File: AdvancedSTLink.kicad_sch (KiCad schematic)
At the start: 66 parts, among them J1 Conn_01x03, J3 Conn_01x06, J4 USB_C_Receptacle_USB2.0, J5 Conn_01x05, Q1 S8050, SW1 SW_SPDT, SW2 SW_Push, U1 STM32F205RETx, U2 XC6206P332MR, U3 USBLC6-2P6, U4 GM9038, U5 USBLC6-2P6, U6 USBLC6-2P6, U7 CH340E, Y1 X322512MSB4SI

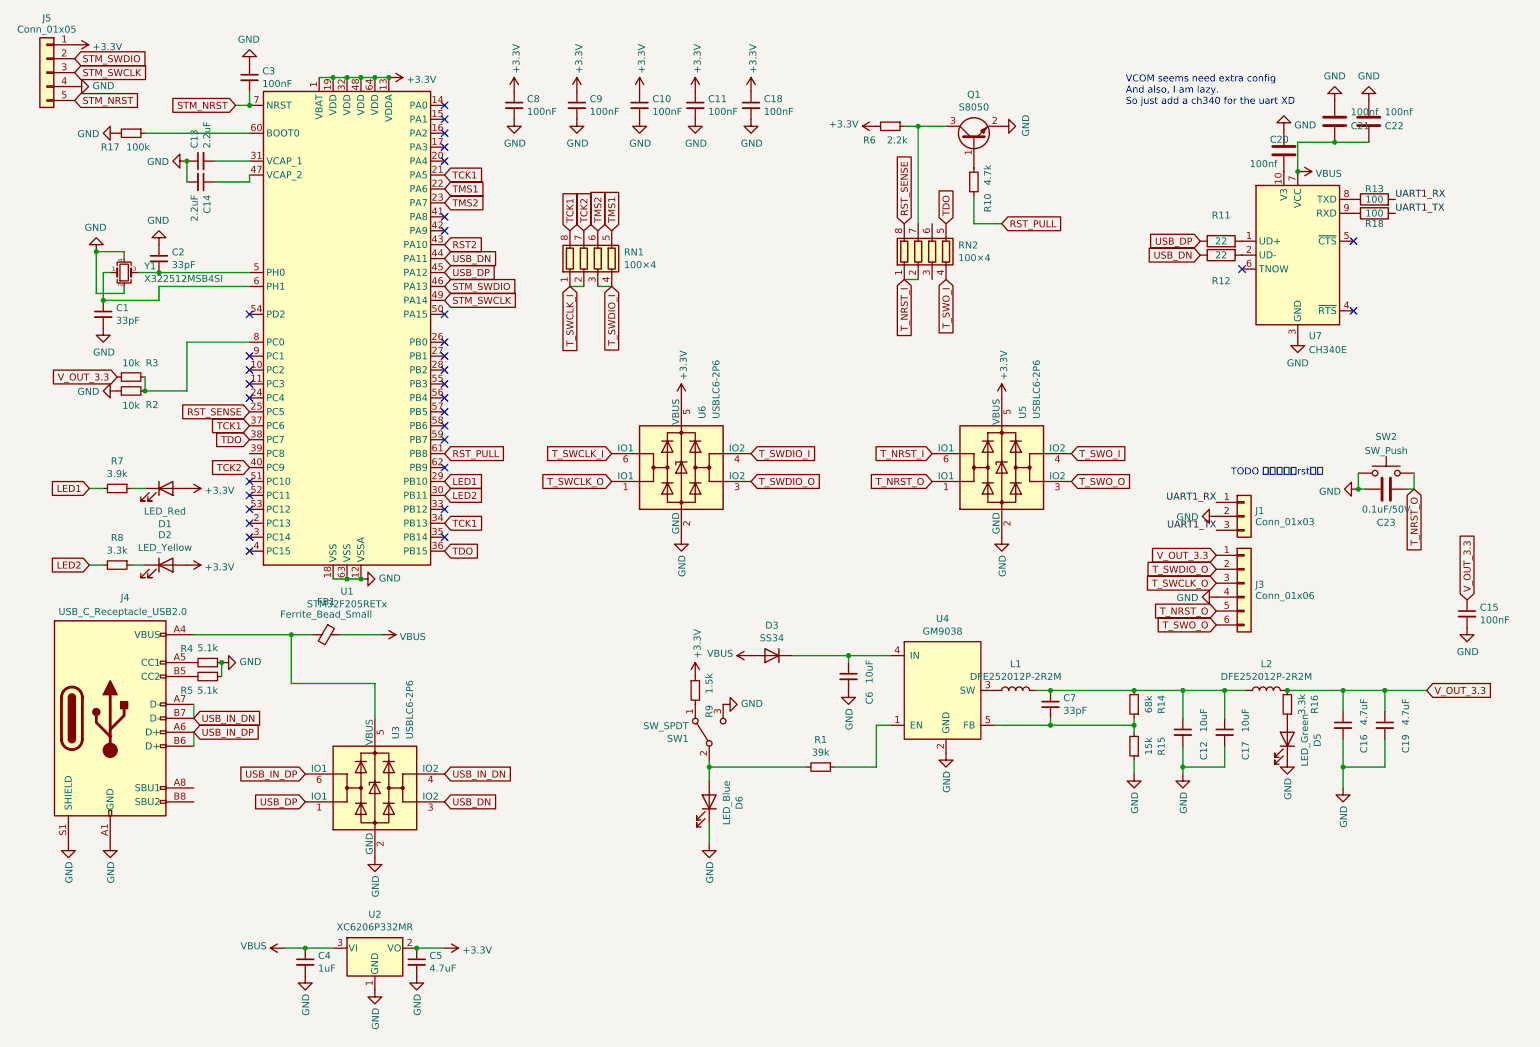
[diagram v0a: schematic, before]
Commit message: Remove CH340, use VCOM
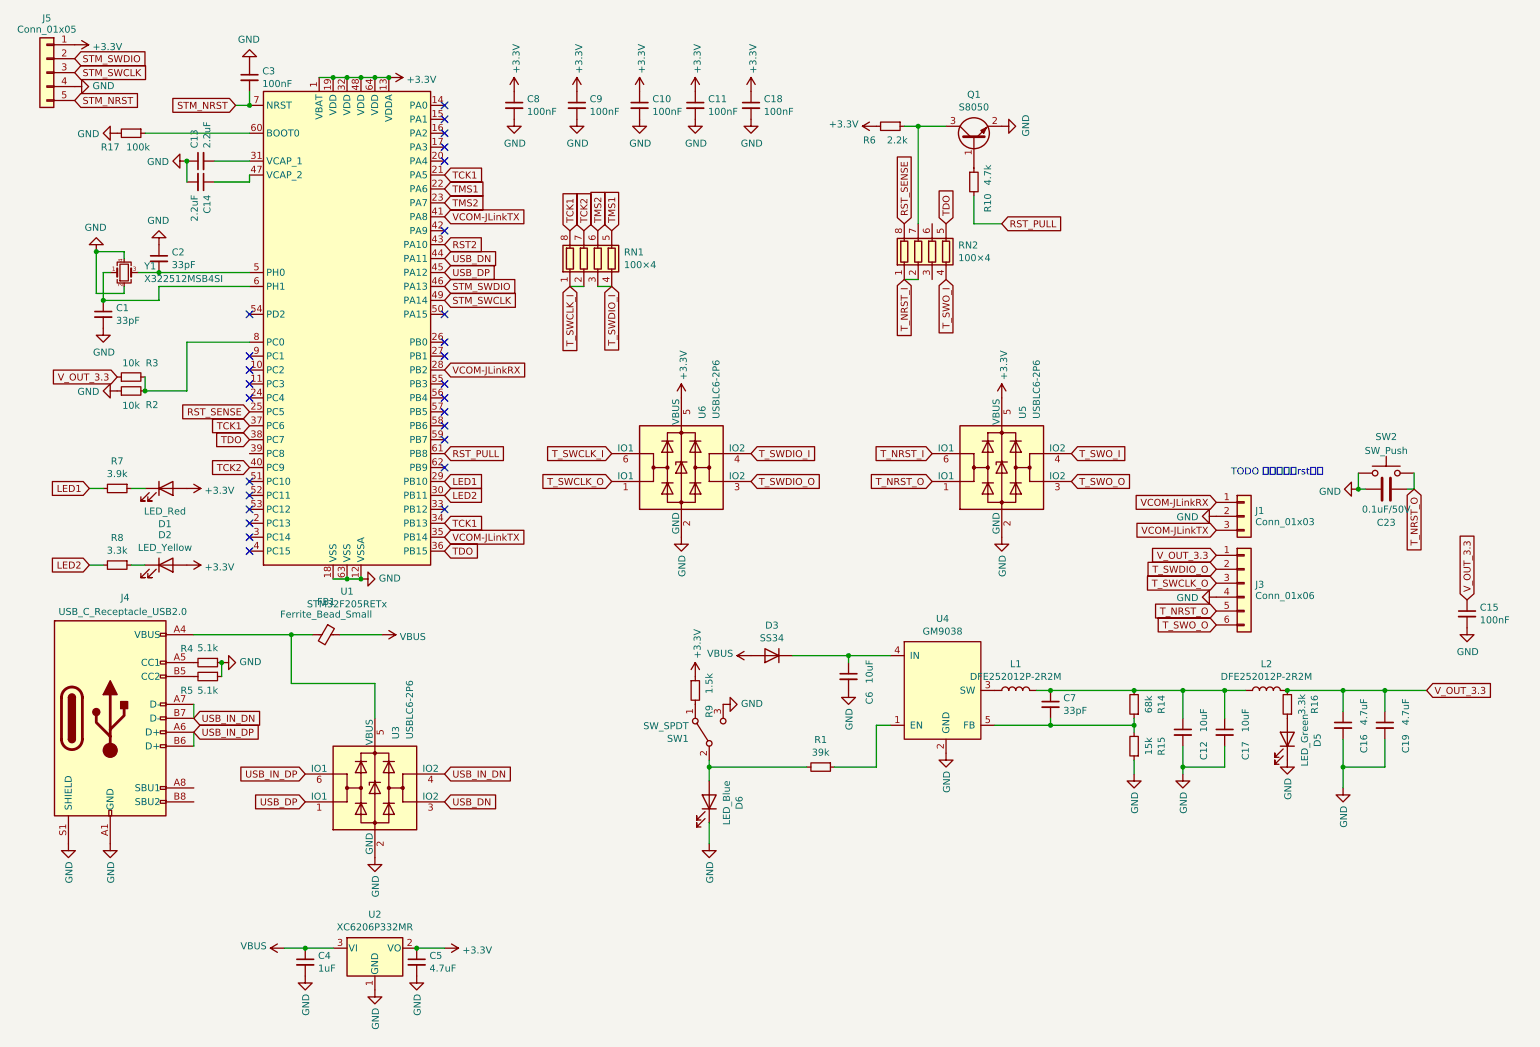
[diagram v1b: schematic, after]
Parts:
- removed C20, C21, C22: 100nf, Capacitor_SMD:C_0402_1005Metric, symbol Device:C
- removed R11, R12: 22, Resistor_SMD:R_0402_1005Metric, symbol Device:R
- removed R13, R18: 100, Resistor_SMD:R_0402_1005Metric, symbol Device:R
- removed U7: CH340E, Package_SO:MSOP-10_3x3mm_P0.5mm, symbol Interface_USB:CH340E
- SW2: footprint KisonNew:C393942 -> Button_Switch_SMD:SW_SPST_CK_RS282G05A3
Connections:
- net UART1_RX is gone; now on net VCOM-JLinkRX: J1.1 (Pin_1)
- net UART1_TX is gone; now on net VCOM-JLinkTX: J1.3 (Pin_3)
- net VCOM-JLinkRX: now reaches U1.28 (PB2)
- net VCOM-JLinkTX: now reaches U1.35 (PB14)
- net VCOM-JLinkTX: now also U1.41 (PA8)
- no-connect marks 33 -> 27
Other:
- note removed: "VCOM seems need extra config And also, I am lazy. So just add a ch340 for the uart XD"

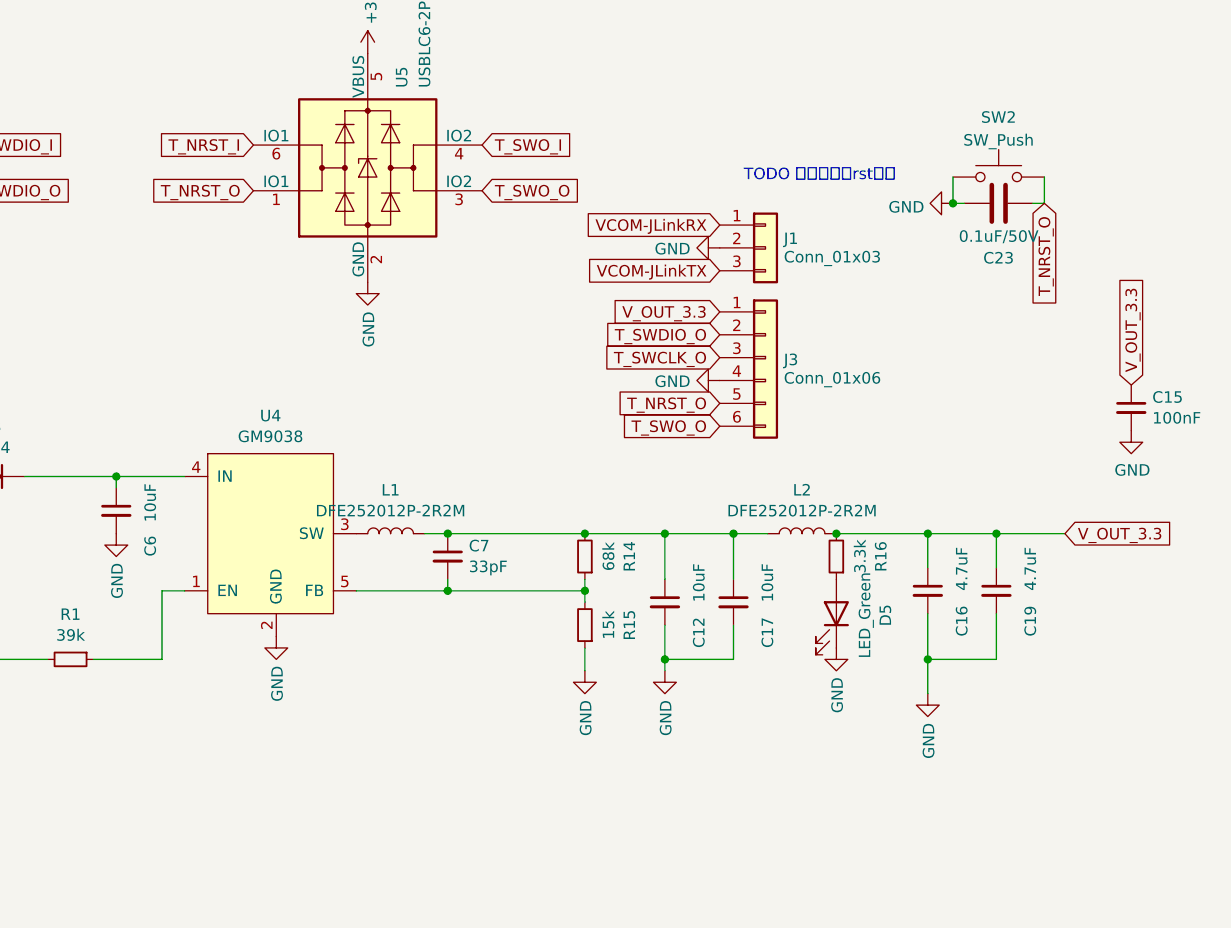
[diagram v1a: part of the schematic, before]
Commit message: Change 3V3 out DCDC to SY8032E
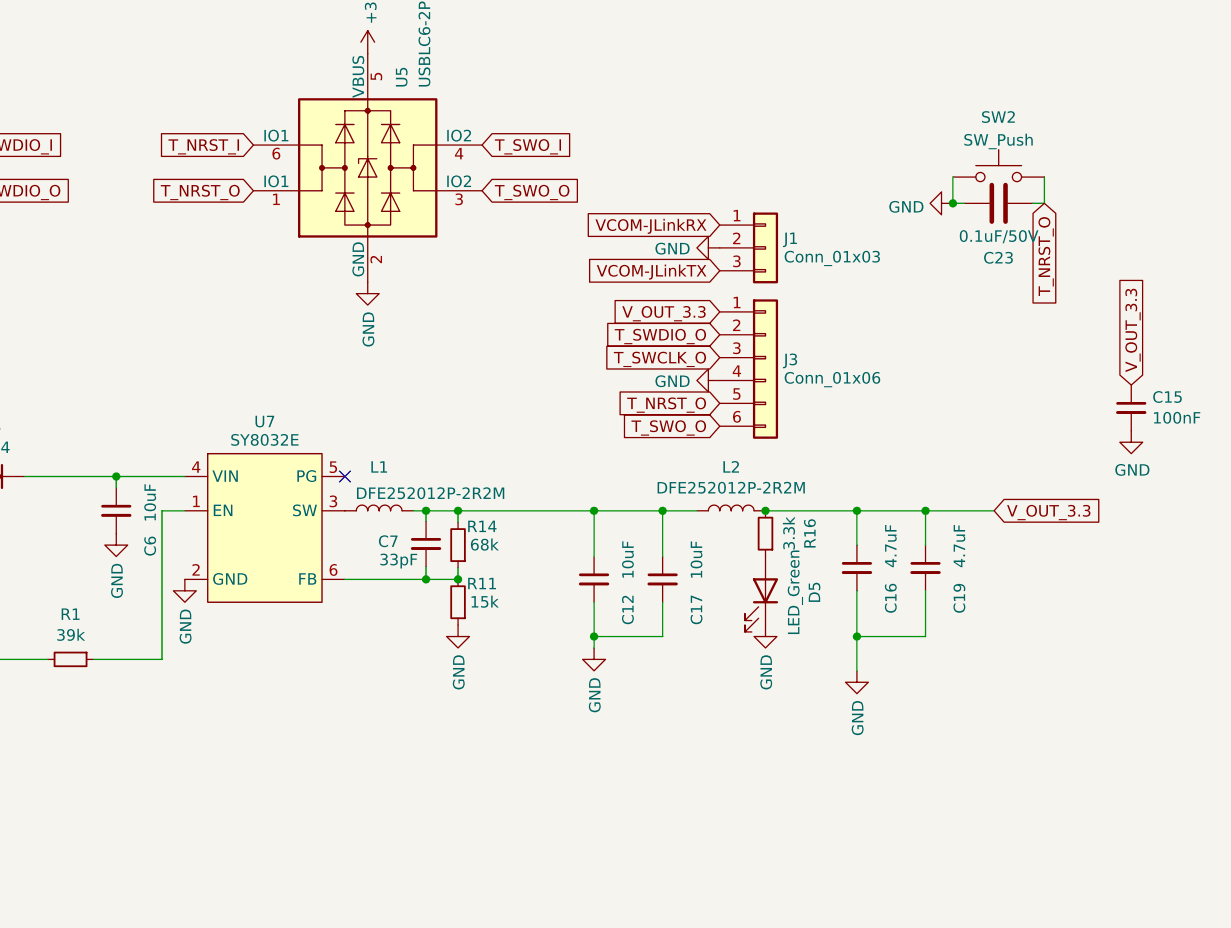
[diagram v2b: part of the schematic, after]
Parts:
- removed R15: 15k, Resistor_SMD:R_0402_1005Metric, symbol Device:R_Small
- removed U4: GM9038, lc:SOT-23-5, symbol MP2359:GM9038
- added R11: 15k, Resistor_SMD:R_0603_1608Metric, symbol Device:R_Small
- added U7: SY8032E, lc:SOT-23-6, symbol t123yh_lib2:SY8032E
- R14: footprint Resistor_SMD:R_0402_1005Metric -> Resistor_SMD:R_0603_1608Metric
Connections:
- net GND: now also R11.1, U7.2 (GND)
- net at C6.1, D3.1 (K): now also U7.4 (VIN)
- net at L1.1: now also U7.3 (SW)
- net at C7.2, R14.1: now also R11.2, U7.6 (FB)
- net at R1.1: now also U7.1 (EN)
- no-connect marks 27 -> 28
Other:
- note removed: "TODO 加一个手动rst开关"
- moved on the sheet: C12, C16, C17, C19, C7, D5, L1, L2, R14, R16

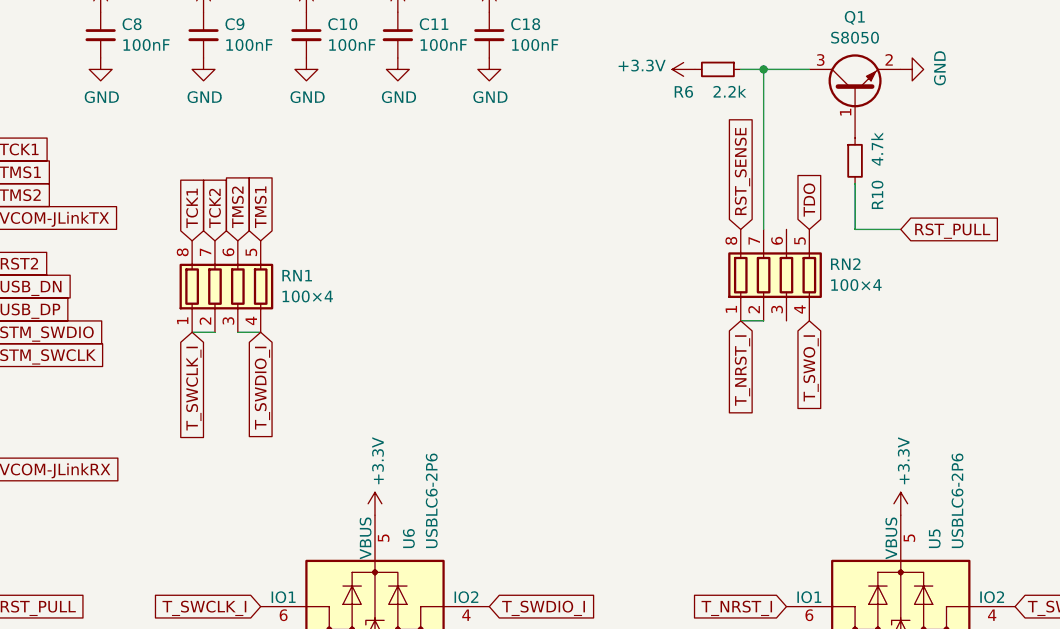
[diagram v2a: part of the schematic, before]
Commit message: 更换排阻为0402, 去除Ref丝印，修正VCOM提示丝印方向
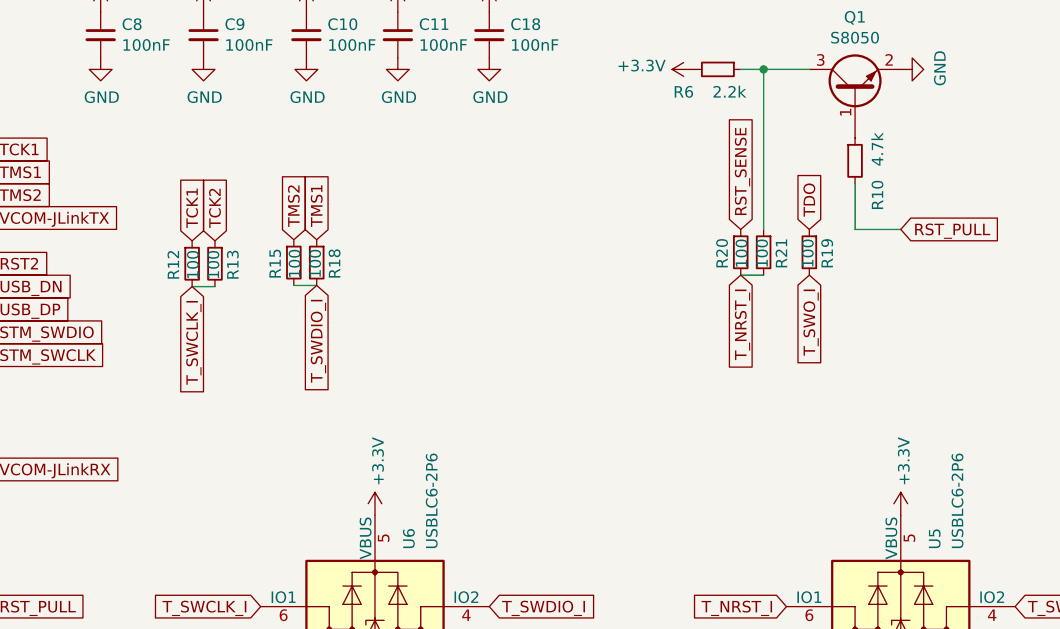
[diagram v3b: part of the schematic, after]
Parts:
- removed RN1, RN2: 100×4, lc:0402_RX4, symbol Device:R_Pack04
- added R12, R13, R15, R18, R19, R20, R21: 100, Resistor_SMD:R_0402_1005Metric, symbol Device:R_Small
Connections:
- net RST_SENSE: now also R20.1
- net TCK1: now also R12.1
- net TCK2: now also R13.1
- net TDO: now also R19.1
- net TMS1: now also R18.1
- net TMS2: now also R15.1
- net T_NRST_I: now also R20.2, R21.2
- net T_SWCLK_I: now also R12.2, R13.2
- net T_SWDIO_I: now also R15.2, R18.2
- net T_SWO_I: now also R19.2
- net at Q1.3 (C), R6.1: now also R21.1

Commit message: 增加一个hub
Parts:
- removed C12, C17: 10uF, Capacitor_SMD:C_0805_2012Metric, symbol Device:C_Small
- removed C16: 4.7uF, Capacitor_SMD:C_0603_1608Metric, symbol Device:C_Small
- removed D5: LED_Green, LED_SMD:LED_0603_1608Metric_Pad1.05x0.95mm_HandSolder, symbol Device:LED
- removed J1: Conn_01x03, Connector_PinHeader_2.54mm:PinHeader_1x03_P2.54mm_Vertical, symbol Connector_Generic:Conn_01x03
- removed L1, L2: DFE252012P-2R2M, lc:DFE252012P, symbol Device:L
- removed R1: 39k, Resistor_SMD:R_0402_1005Metric, symbol Device:R_Small
- removed R11: 15k, Resistor_SMD:R_0603_1608Metric, symbol Device:R_Small
- removed R14: 68k, Resistor_SMD:R_0603_1608Metric, symbol Device:R_Small
- removed R16: 3.3k, Resistor_SMD:R_0402_1005Metric, symbol Device:R_Small
- removed SW1: SW_SPDT, Button_Switch_SMD:SW_SPDT_CK-JS102011SAQN, symbol Switch:SW_SPDT
- removed U7: SY8032E, lc:SOT-23-6, symbol t123yh_lib2:SY8032E
- added C12, C16, C17: 100nf, Capacitor_SMD:C_0402_1005Metric, symbol Device:C
- added C20, C21: 10uf, Capacitor_SMD:C_0805_2012Metric, symbol Device:C
- added H1: MountingHole_Pad, MountingHole:MountingHole_2.2mm_M2_Pad_Via, symbol Mechanical:MountingHole_Pad
- added J2: Conn_01x02_Pin, Connector_PinHeader_2.54mm:PinHeader_1x02_P2.54mm_Vertical, symbol Connector:Conn_01x02_Pin
- added J6: Conn_01x03_Pin, Connector_PinHeader_2.54mm:PinHeader_1x03_P2.54mm_Vertical, symbol Connector:Conn_01x03_Pin
- added R1, R11: 22, Resistor_SMD:R_0402_1005Metric, symbol Device:R
- added R14, R16: 100, Resistor_SMD:R_0402_1005Metric, symbol Device:R
- added U4: SPX1117-3.3, Package_TO_SOT_SMD:SOT-223-3_TabPin2, symbol Regulator_Linear:AZ1117-3.3
- added U7: SL2.1A, Package_SO:SOP-16_4.4x10.4mm_P1.27mm, symbol Interface_USB:FE1.1s
- added U8: CH340E, Package_SO:MSOP-10_3x3mm_P0.5mm, symbol Interface_USB:CH340E
- added U9: USBLC6-2SC6, lc:SOT-23-6, symbol AdvancedSTLink-rescue:USBLC6-2SC6-Power_Protection
- added Y2: Crystal, KisonNew:C16369, symbol Device:Crystal
- C19: value 4.7uF -> 10uf; footprint Capacitor_SMD:C_0603_1608Metric -> Capacitor_SMD:C_0805_2012Metric
- C6: value 10uF -> 10uf
- C7: value 33pF -> 10uf; footprint Capacitor_SMD:C_0402_1005Metric -> Capacitor_SMD:C_0805_2012Metric
- D3: value SS34 -> D; footprint lc:SMA(DO-214AC)_S1 -> Diode_SMD:D_SOD-323; LCSC C8678 -> C191023
- U3, U5, U6: value USBLC6-2P6 -> USBLC6-2SC6; footprint lc:SOT-666 -> lc:SOT-23-6
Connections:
- net +3V3: now also U9.5 (VBUS); no longer R9.1
- net GND: now also C6.1, C7.1, C12.1, C16.2, C17.2, C20.2, C21.2, H1.1, J6.3 (Pin_3), U4.1 (GND), U7.12 (GND), U8.3 (GND), U9.2 (GND); no longer C6.2
- net T_NRST_I: now also U5.1 (IO1); no longer U5.6 (IO1)
- net T_NRST_O: now also U5.6 (IO1); no longer U5.1 (IO1)
- net T_SWO_I: now also U5.3 (IO2); no longer U5.4 (IO2)
- net T_SWO_O: now also U5.4 (IO2); no longer U5.3 (IO2)
- net USB_DN: now also U3.1 (IO1), U7.9 (DMU); no longer U1.44 (PA11), U3.3 (IO2)
- net USB_DP: now also U3.3 (IO2), U7.10 (DPU); no longer U1.45 (PA12), U3.1 (IO1)
- net USB_IN_DN: now also U3.6 (IO1); no longer U3.4 (IO2)
- net USB_IN_DP: now also U3.4 (IO2); no longer U3.6 (IO1)
- net V_OUT_3.3: now also R9.1, J2.1 (Pin_1); no longer C19.1
- net at R9.2: now also D6.2 (A)
- net +5V: now reaches D3.1 (K)
- net +5V: now also C19.1, C16.1, C17.1, C20.1, U4.3 (VI), U7.11 (VDD5), U8.7 (VCC); no longer C6.1
- net at C7.2: now also U7.14 (VD18)
- net VCOM-JLinkRX: no longer names the net of U1.28 (PB2)
- net VCOM-JLinkTX: no longer names the net of U1.35 (PB14)
- net VCOM-JLinkTX: no longer U1.41 (PA8)
- new net: R14.1, U8.8 (TXD)
- new net: C21.1, J2.2 (Pin_2), U4.2 (VO)
- new net: C12.2, U8.10 (V3)
- new net: R11.1, U7.1 (DM4)
- new net: R11.2, U8.2 (UD-)
- new net: C6.2, U7.13 (VD33)
- new net: R1.2, U8.1 (UD+)
- new net: R16.2, U8.9 (RXD)
- new net: U7.16 (XIN), Y2.1
- new net: U7.15 (XOUT), Y2.2
- new net: R1.1, U7.2 (DP4)
- new net MCU_USB_DN: U1.44 (PA11), U7.8 (DP1)
- new net MCU_USB_DP: U1.45 (PA12), U7.7 (DM1)
- new net RX_I: R16.1, U9.4 (IO2)
- new net RX_O: J6.2 (Pin_2), U9.3 (IO2)
- new net TX_I: R14.2, U9.6 (IO1)
- new net TX_O: J6.1 (Pin_1), U9.1 (IO1)
- no-connect marks 28 -> 33
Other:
- note added: "上位机串口"
- note added: "电源"
- moved on the sheet: D6, J3, R9, U5, U6

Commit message: 更新原理图
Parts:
- removed C12, C16, C17: 100nf, Capacitor_SMD:C_0402_1005Metric, symbol Device:C
- removed C19, C6, C7: 10uf, Capacitor_SMD:C_0805_2012Metric, symbol Device:C_Small
- removed D3: D, Diode_SMD:D_SOD-323, symbol Device:D
- removed J6: Conn_01x03_Pin, Connector_PinHeader_2.54mm:PinHeader_1x03_P2.54mm_Vertical, symbol Connector:Conn_01x03_Pin
- removed R1, R11: 22, Resistor_SMD:R_0402_1005Metric, symbol Device:R
- removed R14, R16: 100, Resistor_SMD:R_0402_1005Metric, symbol Device:R
- removed U7: SL2.1A, Package_SO:SOP-16_4.4x10.4mm_P1.27mm, symbol Interface_USB:FE1.1s
- removed U8: CH340E, Package_SO:MSOP-10_3x3mm_P0.5mm, symbol Interface_USB:CH340E
- removed U9: USBLC6-2SC6, lc:SOT-23-6, symbol AdvancedSTLink-rescue:USBLC6-2SC6-Power_Protection
- removed Y2: Crystal, KisonNew:C16369, symbol Device:Crystal
- added H2, H3, H4: MountingHole_Pad, MountingHole:MountingHole_2.2mm_M2_Pad_Via, symbol Mechanical:MountingHole_Pad
- added J1: Conn_01x03, Connector_PinHeader_2.54mm:PinHeader_1x03_P2.54mm_Vertical, symbol Connector_Generic:Conn_01x03
- added U7: USBLC6-2SC6, lc:SOT-23-6, symbol AdvancedSTLink-rescue:USBLC6-2SC6-Power_Protection
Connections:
- net MCU_USB_DN is gone; now on net USB_DN: U1.44 (PA11)
- net MCU_USB_DP is gone; now on net USB_DP: U1.45 (PA12)
- net +3V3: now also U7.5 (VBUS)
- net GND: now also H2.1, H3.1, H4.1, J1.2 (Pin_2), U7.2 (GND)
- net VCOM-JLinkRX: now reaches U1.28 (PB2)
- net VCOM-JLinkRX: now also U7.6 (IO1)
- net VCOM-JLinkTX: now reaches U1.35 (PB14)
- net VCOM-JLinkTX: now also U7.4 (IO2)
- new net VCOM-RX: J1.3 (Pin_3), U7.1 (IO1)
- new net VCOM-TX: J1.1 (Pin_1), U7.3 (IO2)
- no-connect marks 33 -> 28
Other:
- note added: "对外电源"
- note removed: "上位机串口"
- note removed: "电源"
- moved on the sheet: C1, C10, C11, C13, C14, C15, C18, C2, C20, C21, C23, C3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
